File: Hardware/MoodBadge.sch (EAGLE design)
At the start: 80 parts, among them IC1 PCF8574T, U2 ATMEGA328P_TQFP, Y1 Crystal-CA-310

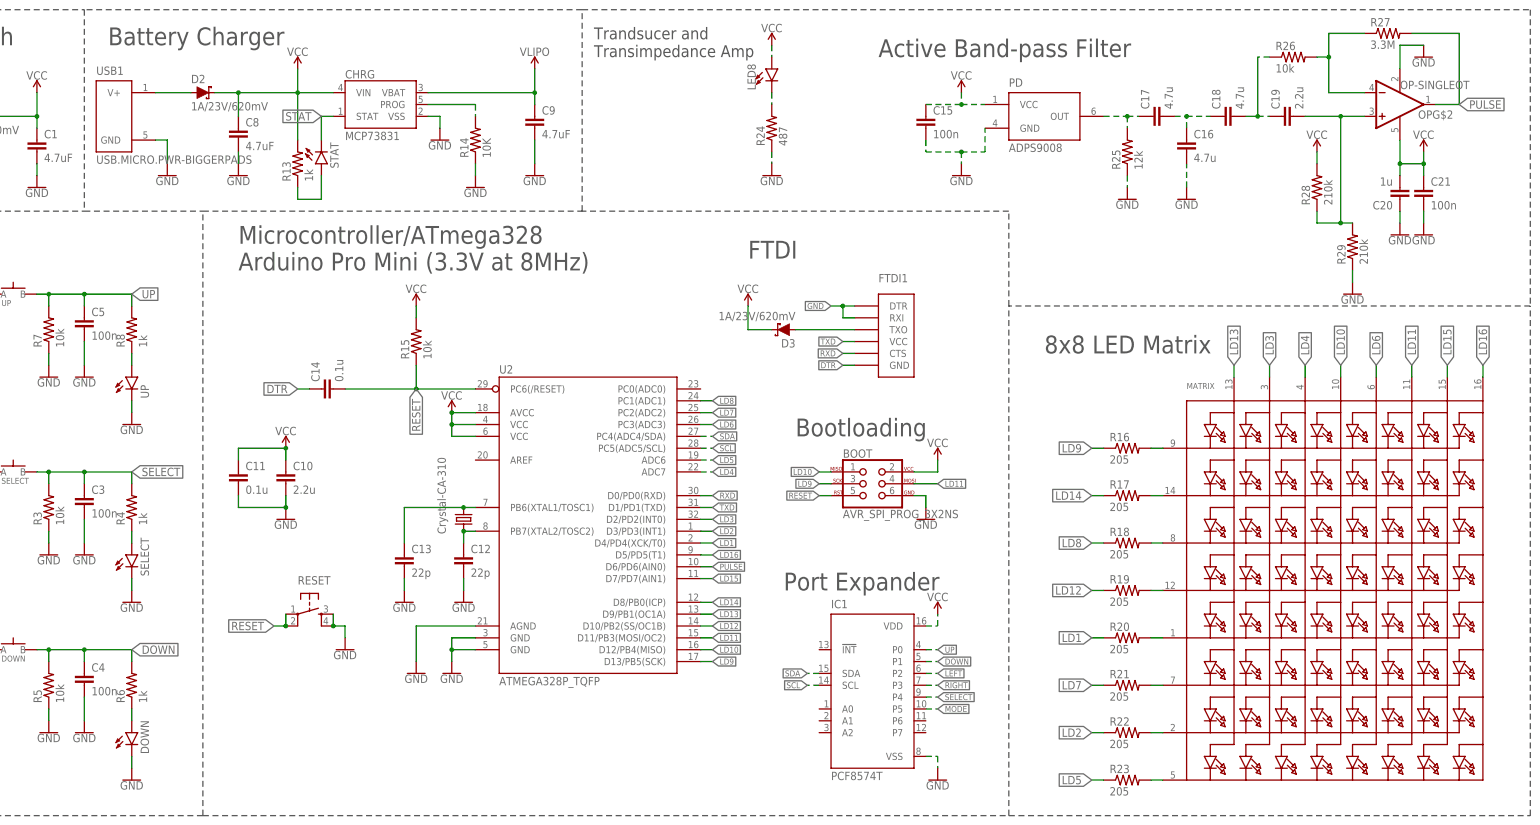
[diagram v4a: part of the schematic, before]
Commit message: Added title block
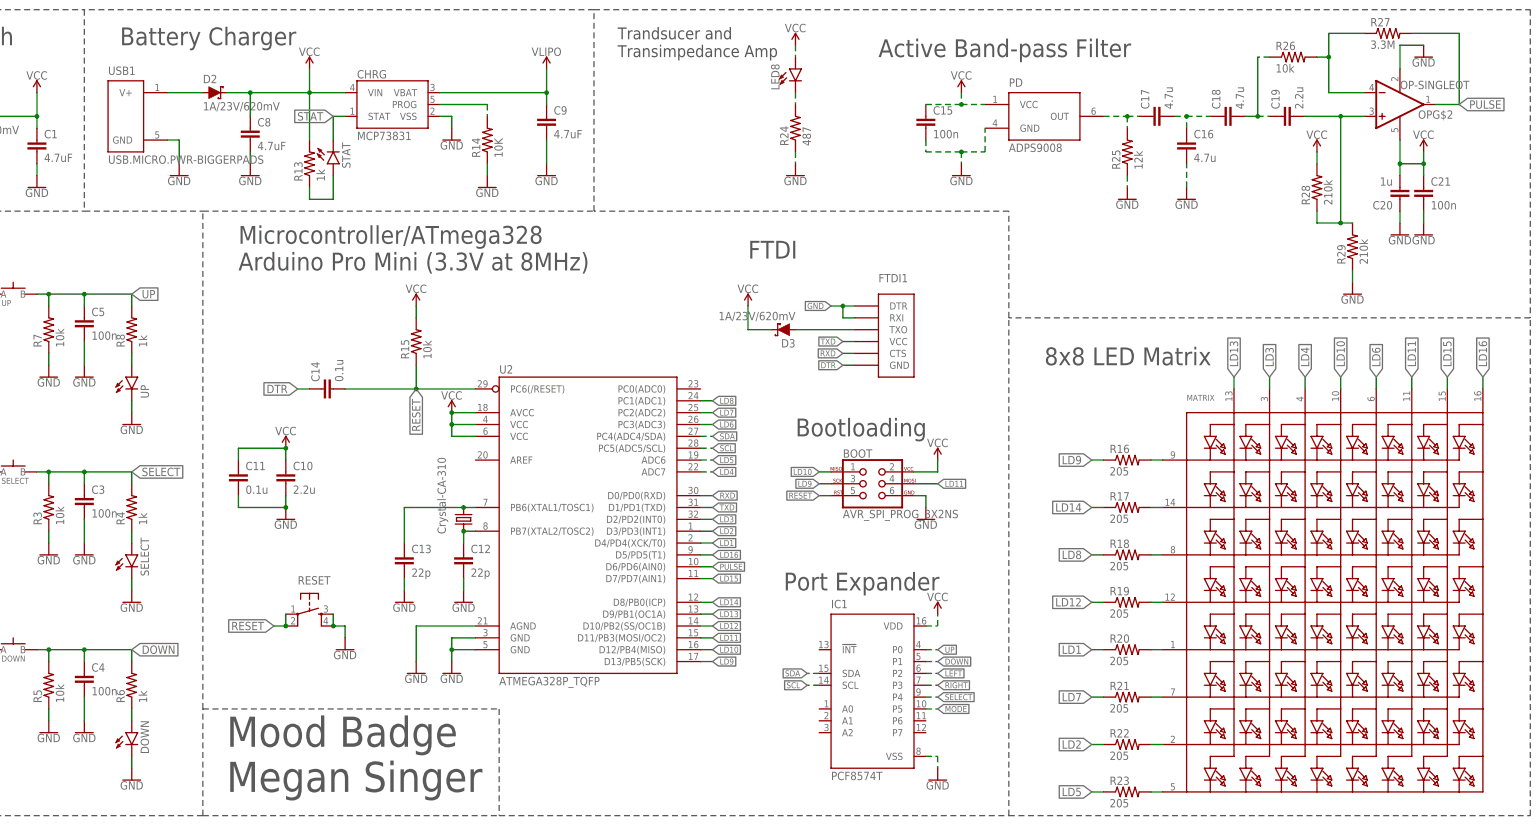
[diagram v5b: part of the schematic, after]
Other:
- note added: "Mood Badge Megan Singer"
- moved on the sheet: C8, C9, CHRG, D2, LED8, MATRIX, R13, R14, R16, R17, R18, R19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

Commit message: Continued routing and changed a few pins for easier routing
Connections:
- net RIGHT: now also IC1.P0; no longer IC1.P3
- net UP: now also IC1.P3; no longer IC1.P0
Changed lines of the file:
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@@
 </segment>
 <segment>
-<pinref part="IC1" gate="G$1" pin="P0"/>
-<wire x1="259.08" y1="35.56" x2="261.62" y2="35.56" width="0.1524" layer="91" style="longdash"/>
-<label x="261.62" y="35.56" size="1.27" layer="95" xref="yes"/>
+<pinref part="IC1" gate="G$1" pin="P3"/>
+<wire x1="259.08" y1="27.94" x2="261.62" y2="27.94" width="0.1524" layer="91"/>
+<label x="261.62" y="27.94" size="1.27" layer="95" xref="yes"/>
 </segment>
 </net>
@@
 </segment>
 <segment>
-<pinref part="IC1" gate="G$1" pin="P3"/>
-<wire x1="259.08" y1="27.94" x2="261.62" y2="27.94" width="0.1524" layer="91" style="longdash"/>
-<label x="261.62" y="27.94" size="1.27" layer="95" xref="yes"/>
+<pinref part="IC1" gate="G$1" pin="P0"/>
+<wire x1="259.08" y1="35.56" x2="261.62" y2="35.56" width="0.1524" layer="91"/>
+<label x="261.62" y="35.56" size="1.27" layer="95" xref="yes"/>
 </segment>
 </net>

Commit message: Fixed labeling error for FTDI pins
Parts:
- removed FTDI1: FTDI_DEVICE, LinnesLab-Connectors:FTDI_DEVICE
- added FTDI2: FTDI_DEVICE, LinnesLab-Connectors:FTDI_DEVICE
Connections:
- net DTR: now also FTDI2.DTR; no longer FTDI1.GND
- net GND: now also FTDI2.CTS, FTDI2.GND; no longer FTDI1.DTR, FTDI1.RXI
- net N$12: now also FTDI2.VCC; no longer FTDI1.TXO
- net RXD: now also FTDI2.RXI; no longer FTDI1.CTS
- net TXD: now also FTDI2.TXO; no longer FTDI1.VCC
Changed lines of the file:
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@@
 <part name="RESET" library="LinnesLab-Switches" deviceset="SPST-PTS830GG140" device="" package3d_urn="urn:adsk.eagle:package:18580190/2"/>
 <part name="D3" library="LinnesLab-DiscreteSemi" deviceset="SCHOTTKY" device="-USC" package3d_urn="urn:adsk.eagle:package:15664784/2" value="1A/23V/620mV"/>
-<part name="FTDI1" library="LinnesLab-Connectors" deviceset="FTDI_DEVICE" device=""/>
 <part name="BOOT" library="LinnesLab-Connectors" deviceset="AVR_SPI_PROG_3X2" device="NS" package3d_urn="urn:adsk.eagle:package:18167648/2"/>
 <part name="GND32" library="LinnesLab-Symbols" deviceset="GND" device=""/>
@@
 <part name="GND41" library="LinnesLab-Symbols" deviceset="GND" device=""/>
 <part name="OP" library="LinnesLab-AnalogIC" deviceset="OP-SINGLE" device="OT" package3d_urn="urn:adsk.eagle:package:18172171/2" value="OP-SINGLEOT"/>
+<part name="FTDI2" library="LinnesLab-Connectors" deviceset="FTDI_DEVICE" device=""/>
 </parts>
 <sheets>
@@
 <attribute name="VALUE" x="231.14" y="106.172" size="1.778" layer="96" font="vector" rot="R180" align="top-left"/>
 </instance>
-<instance part="FTDI1" gate="G$1" x="248.92" y="104.14" smashed="yes">
-<attribute name="NAME" x="248.92" y="114.3" size="1.778" layer="95"/>
-<attribute name="VALUE" x="248.92" y="111.76" size="1.778" layer="96" display="off"/>
-</instance>
 <instance part="BOOT" gate="G$1" x="246.38" y="71.12" smashed="yes">
 <attribute name="NAME" x="241.3" y="76.708" size="1.778" layer="95" font="vector"/>
@@
 <attribute name="NAME" x="372.11" y="151.13" size="1.778" layer="95" rot="R180"/>
 <attribute name="VALUE" x="359.41" y="157.48" size="1.778" layer="96" rot="R180" display="off"/>
+</instance>
+<instance part="FTDI2" gate="G$1" x="248.92" y="101.6" smashed="yes" rot="MR180">
+<attribute name="NAME" x="248.92" y="91.44" size="1.778" layer="95" rot="MR180"/>
+<attribute name="VALUE" x="248.92" y="93.98" size="1.778" layer="96" rot="MR180"/>
 </instance>
 </instances>
@@
 </segment>
 <segment>
-<pinref part="FTDI1" gate="G$1" pin="DTR"/>
 <wire x1="243.84" y1="109.22" x2="241.3" y2="109.22" width="0.1524" layer="91"/>
-<pinref part="FTDI1" gate="G$1" pin="RXI"/>
 <wire x1="241.3" y1="109.22" x2="238.76" y2="109.22" width="0.1524" layer="91"/>
 <wire x1="243.84" y1="106.68" x2="241.3" y2="106.68" width="0.1524" layer="91"/>
@@
 <junction x="241.3" y="109.22"/>
 <label x="238.76" y="109.22" size="1.27" layer="95" rot="R180" xref="yes"/>
+<pinref part="FTDI2" gate="G$1" pin="CTS"/>
+<pinref part="FTDI2" gate="G$1" pin="GND"/>
 </segment>
 <segment>
@@
 </segment>
 <segment>
-<pinref part="FTDI1" gate="G$1" pin="GND"/>
 <wire x1="243.84" y1="96.52" x2="241.3" y2="96.52" width="0.1524" layer="91"/>
 <label x="241.3" y="96.52" size="1.27" layer="95" rot="R180" xref="yes"/>
+<pinref part="FTDI2" gate="G$1" pin="DTR"/>
 </segment>
 </net>
@@
 </segment>
 <segment>
-<pinref part="FTDI1" gate="G$1" pin="CTS"/>
 <wire x1="243.84" y1="99.06" x2="241.3" y2="99.06" width="0.1524" layer="91"/>
 <label x="241.3" y="99.06" size="1.27" layer="95" rot="R180" xref="yes"/>
+<pinref part="FTDI2" gate="G$1" pin="RXI"/>
 </segment>
 </net>
@@
 </segment>
 <segment>
-<pinref part="FTDI1" gate="G$1" pin="VCC"/>
 <wire x1="243.84" y1="101.6" x2="241.3" y2="101.6" width="0.1524" layer="91"/>
 <label x="241.3" y="101.6" size="1.27" layer="95" rot="R180" xref="yes"/>
+<pinref part="FTDI2" gate="G$1" pin="TXO"/>
 </segment>
 </net>
@@
 </segment>
 </net>
-<net name="N$12" class="0">
+<net name="N$12" class="1">
 <segment>
 <pinref part="D3" gate="G$1" pin="A"/>
-<pinref part="FTDI1" gate="G$1" pin="TXO"/>
 <wire x1="231.14" y1="104.14" x2="243.84" y2="104.14" width="0.1524" layer="91"/>
-</segment>
-</net>
+<pinref part="FTDI2" gate="G$1" pin="VCC"/>
+</segment>
+</net>
